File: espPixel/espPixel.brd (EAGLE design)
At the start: 39.3 x 80 mm, 68 parts, among them IC1 74LVC1T45GW,125, IC3 MP2315GJ-Z, IC4 CP2104, J1 TBLH10-350-04BK, J2 TBLH10-350-03BK, J3 TBLH10-350-02BK, Q1 SIR414DP-T1-GE3, Q2 SIR414DP-T1-GE3, Q5 mmbt2222, Q6 mmbt2222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

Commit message: bug fix
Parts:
- L1: value 4uh -> 1.5uh
- moved R11 1.80 mm to (15.7, 5.33), turned to 0 degrees
- moved R10 0.25 mm to (22.6, 4.32)
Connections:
- removed net N$7: C6.2, D1.A, U$1.1, U$1.2
- new net VDD: C6.2, D1.A, R12.1, U$1.1, U$1.2
- net VIN: no longer R12.1
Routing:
- net VDD: track 0.00 -> 14.6 mm, vias 0 -> 2
- net N$7: track 4.16 -> 0.00 mm
- net HSW: track 35.2 -> 31.0 mm, vias 30 -> 42
- net VIN: track 65.4 -> 63.9 mm, vias 52 -> 73
- net N$14: track 3.70 -> 3.15 mm
- net N$15: track 14.3 -> 14.8 mm
- net GND: vias 139 -> 152
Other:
- board text added: "V2.0"
- board text removed: "V1.0"

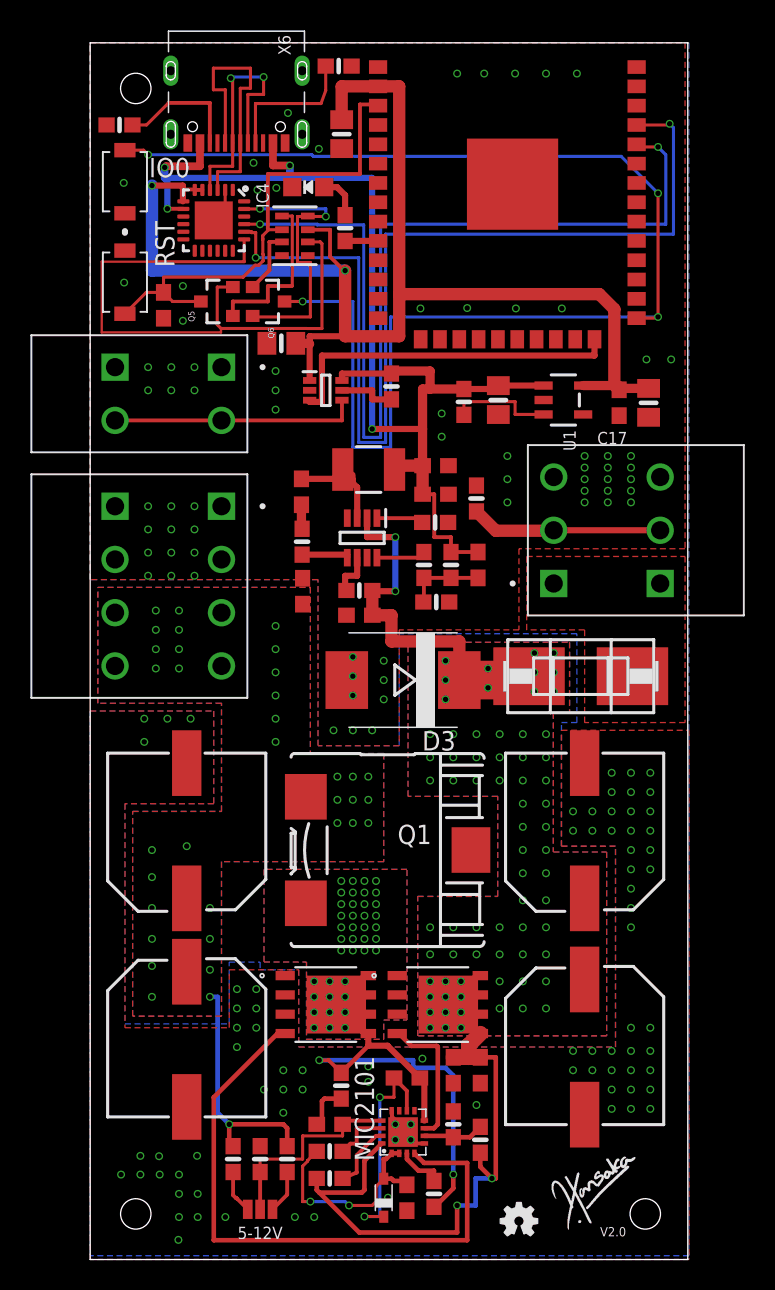
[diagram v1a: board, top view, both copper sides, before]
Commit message: Text clean up
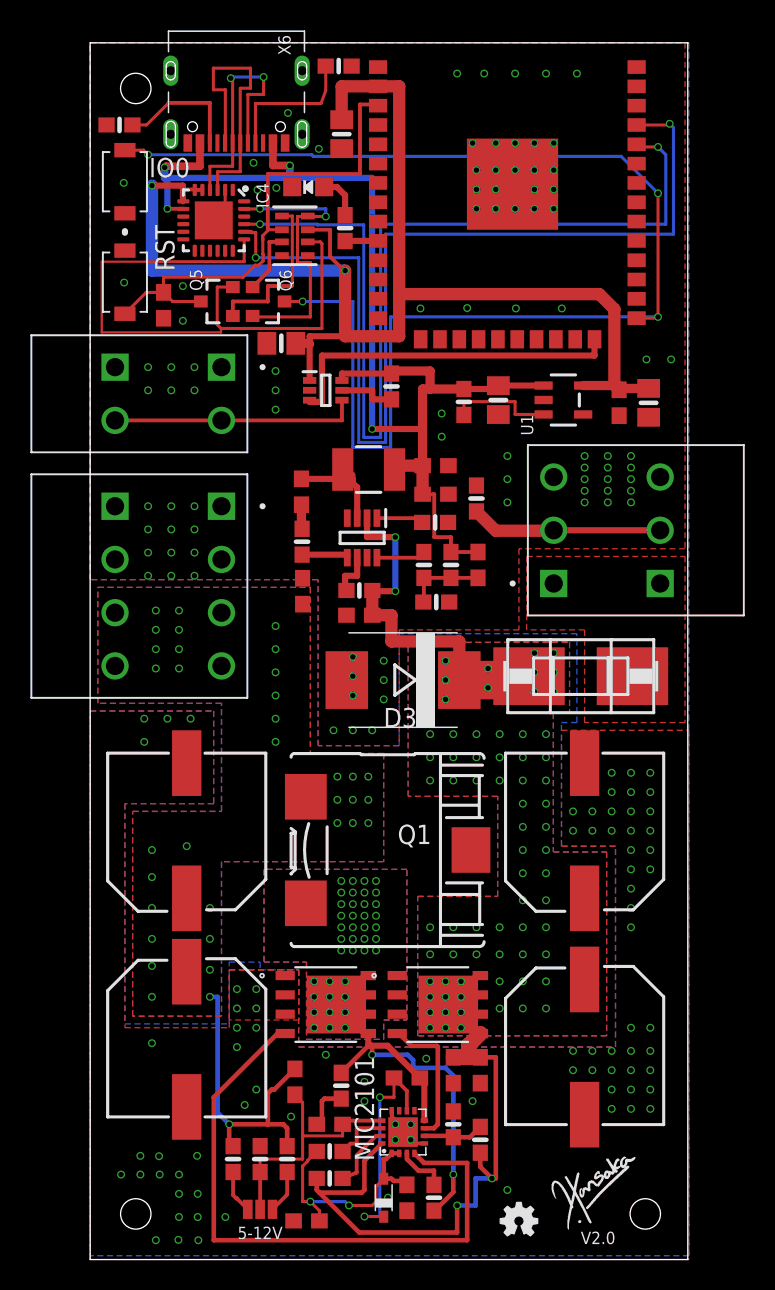
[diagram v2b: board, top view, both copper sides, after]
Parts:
- added C20: 0.4.7nf, microbuilder:0603-NO@1
- added C21: 4.7uf, microbuilder:0603-NO@1
- moved R10 0.25 mm to (22.6, 4.06)
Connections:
- net GND: now also C21.1
- net N$11: now also C20.1
- net VDD: now also C21.2
- net VOUT: now also C20.2
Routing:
- net VOUT: track 16.4 -> 20.8 mm
- net HSW: track 31.0 -> 26.7 mm
- net GND: track 5.91 -> 8.96 mm, vias 152 -> 171
- net N$11: track 13.7 -> 16.6 mm
- net VDD: track 14.6 -> 16.1 mm

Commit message: tunining
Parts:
- C20: value 0.4.7nf -> 4.7nf
- L1: value 1.5uh -> 4.7uh
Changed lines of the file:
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@@
 <attribute name="MOUSER_PRICE-STOCK" value="https://www.mouser.co.uk/ProductDetail/Nexperia/74LVC1T45GW125?qs=jquClx72t9Aoi%252BsTRKaaAg%3D%3D" x="37.084" y="10.16" size="1.778" layer="27" display="off"/>
 </element>
-<element name="L1" library="rcl" library_urn="urn:adsk.eagle:library:334" package="CEP125" package3d_urn="urn:adsk.eagle:package:25968/1" value="1.5uh" x="19.558" y="26.924" smashed="yes" rot="R90">
+<element name="L1" library="rcl" library_urn="urn:adsk.eagle:library:334" package="CEP125" package3d_urn="urn:adsk.eagle:package:25968/1" value="4.7uh" x="19.558" y="26.924" smashed="yes" rot="R90">
 <attribute name="POPULARITY" value="0" x="27.178" y="47.244" size="1.778" layer="27" rot="R90" display="off"/>
 <attribute name="SPICEPREFIX" value="L" x="27.178" y="47.244" size="1.778" layer="27" rot="R90" display="off"/>
@@
 <attribute name="PRICE" value="None" x="2.286" y="70.866" size="1.778" layer="27" rot="R90" display="off"/>
 </element>
-<element name="C20" library="microbuilder" package="0603-NO@1" value="0.4.7nf" x="13.462" y="11.684" smashed="yes" rot="R90">
+<element name="C20" library="microbuilder" package="0603-NO@1" value="4.7nf" x="13.462" y="11.684" smashed="yes" rot="R90">
 <attribute name="VALUE" x="12.7" y="9.906" size="0.8128" layer="27" font="vector" ratio="10" rot="R90"/>
 </element>

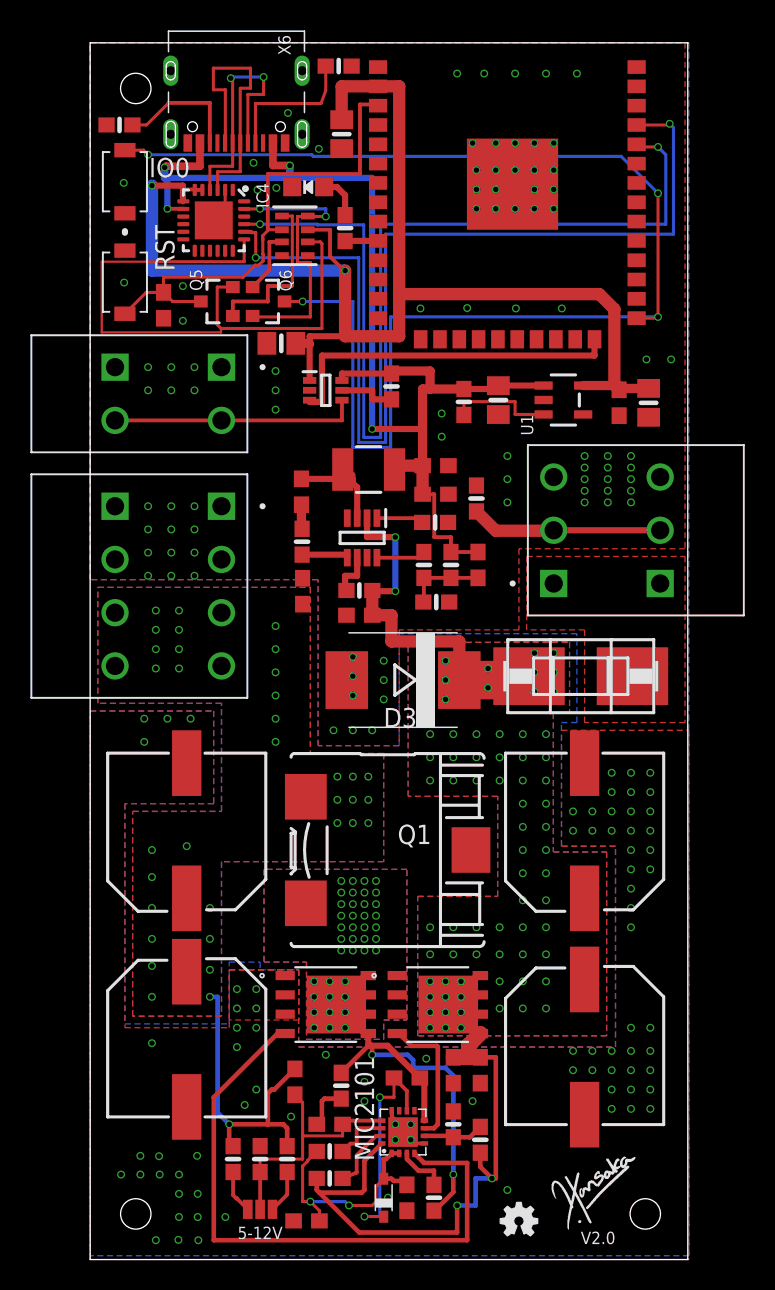
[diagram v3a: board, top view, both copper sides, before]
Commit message: ability to turn off the output
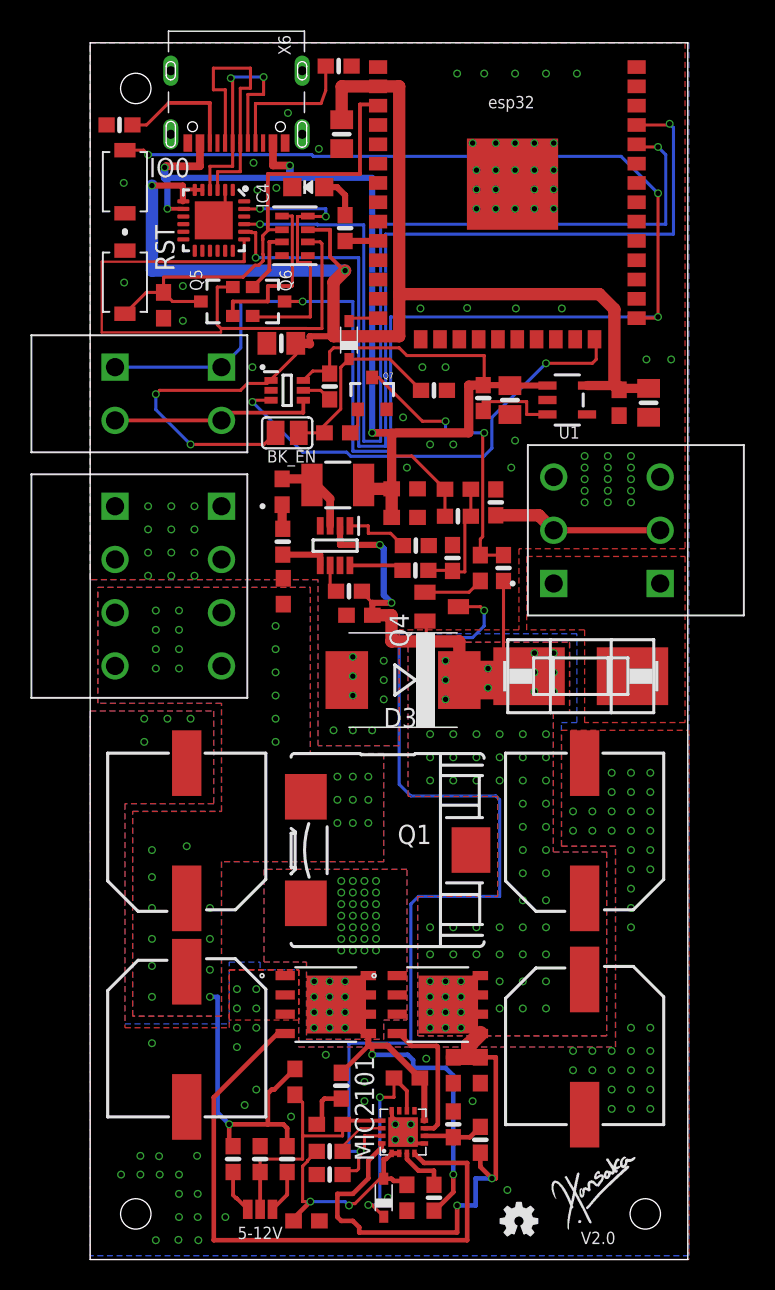
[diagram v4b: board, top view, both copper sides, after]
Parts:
- added BK_EN: (no value), jumper:SJ
- added D2: BAT60J, diode:SOD323_ST
- added Q4: (no value), semicon-smd-ipc:SOT23
- added Q7: mmbt2222, SparkFun:SOT23-3
- added R19: 1.2k, SparkFun-Resistors:0603
- added R20, R24, R25: 100K, microbuilder:0603-NO
- R16: value 50K -> 10
- R6: value 100K -> 1.2k; device microbuilder:0603-NO -> SparkFun-Resistors:0603
- moved R11 38.6 mm to (17.0, 43.9), turned to 180 degrees
- moved R6 10.5 mm to (16.3, 54.4)
- moved C10 5.15 mm to (24.2, 50.6), turned to 0 degrees
- moved R18 4.06 mm to (15.7, 57.4)
- moved R3 3.23 mm to (24.2, 48.9), turned to 0 degrees
- moved R4 3.09 mm to (23.8, 46.1), turned to 90 degrees
- moved C2 2.54 mm to (20.7, 50.7)
- moved C8 2.54 mm to (20.7, 48.8)
- moved IC1 2.54 mm to (13.0, 57.1)
- moved L3 2.27 mm to (16.3, 50.9)
- moved R1 1.98 mm to (21.4, 46.9)
- moved IC3 1.85 mm to (16.1, 46.9)
- moved R16 1.30 mm to (26.7, 49.8)
- moved R17 1.30 mm to (25.8, 56.6)
- moved C4 1.27 mm to (12.7, 43.9)
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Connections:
- removed net N$16: R11.2, U$1.15
- new net BUCK_EN: Q4.3, R25.1, U$1.15
- new net GPIO12: D2.A, X8.14
- new net N$23: Q7.1, R6.1
- new net N$24: Q4.1, R19.1
- new net N$26: Q7.3, R19.2, R24.1
- new net N$9: BK_EN.1, D2.C, R20.2, R6.2
- net 3.3V: now also BK_EN.2
- net GND: now also Q7.2, R20.1, R25.2; no longer J3.1_A, J3.1_B
- net GPIO0: now also J3.1_A, J3.1_B
- net N$5: now also R11.2; no longer R6.2
- net VIN: now also Q4.2, R24.2; no longer R6.1
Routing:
- net BUCK_EN: track 0.00 -> 63.4 mm, vias 0 -> 2
- net 3.3V: track 90.6 -> 110.0 mm, vias 2 -> 4
- net N$26: track 0.00 -> 19.0 mm, vias 0 -> 2
- net GPIO0: track 88.6 -> 105.0 mm
- net N$9: track 0.00 -> 12.9 mm
- net VBUS: track 76.8 -> 85.9 mm
- net NEODATA_3V: track 23.0 -> 30.6 mm, vias 0 -> 2
- net VIN: track 63.9 -> 71.2 mm
- net N$16: track 4.32 -> 0.00 mm
- net N$24: track 0.00 -> 3.95 mm
- net N$2: track 5.18 -> 8.29 mm
- net NEODATA_5V: track 16.2 -> 13.4 mm
- net GPIO12: track 0.00 -> 1.99 mm
- net N$22: track 3.85 -> 1.98 mm
- net N$23: track 0.00 -> 1.74 mm
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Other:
- board text added: "5V|12V"
- board text added: "8V-24V"
- board text added: "CK"
- board text added: "DATA"
- board text added: "GND"
- board text added: "PW-EN"
- board text added: "esp32"

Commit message: bigger caps
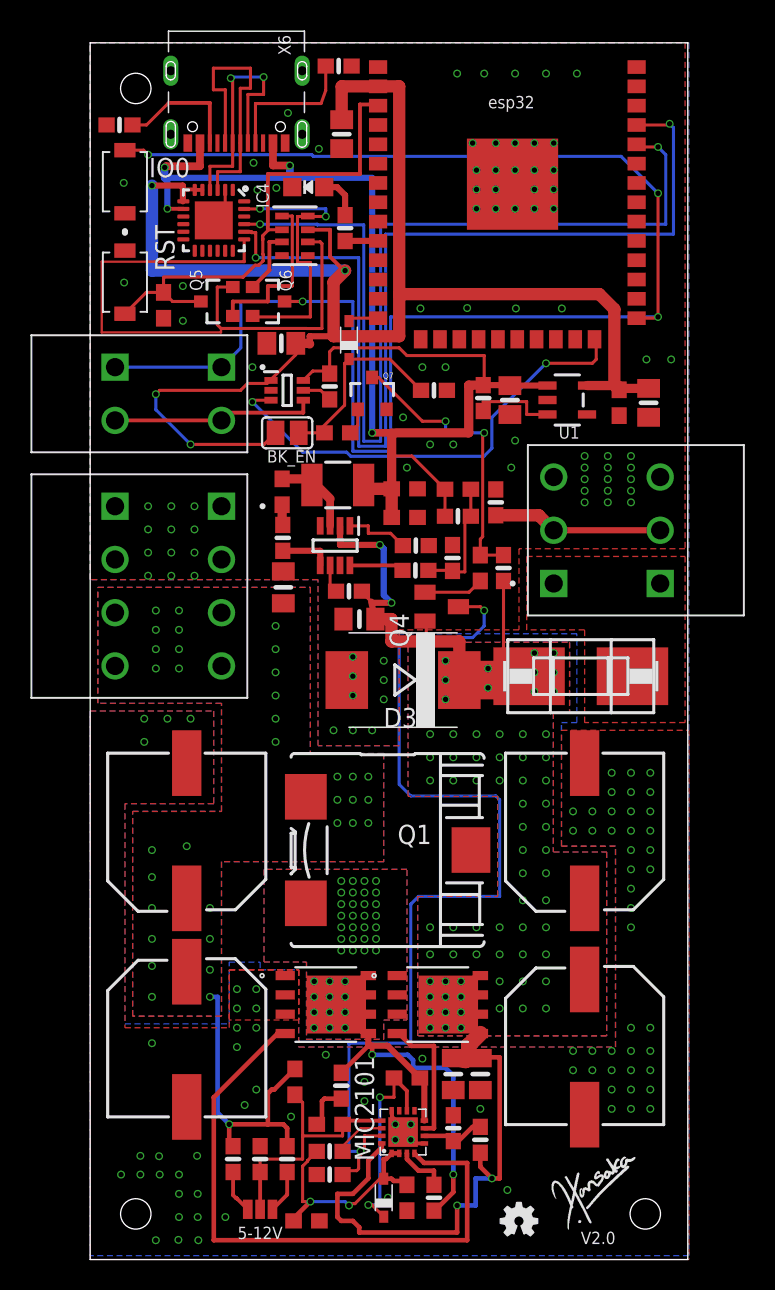
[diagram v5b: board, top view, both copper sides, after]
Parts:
- C12, C4, C7, C9: device microbuilder:0603-NO@1 -> microbuilder:0805_10MGAP
- moved C9 0.25 mm to (17.7, 42.1)
- moved R5 0.25 mm to (12.7, 47.5)
- moved R14 0.25 mm to (23.9, 8.64)
- moved C12 0.25 mm to (25.7, 12.2)
- moved C7 0.25 mm to (23.9, 12.2)
- moved C4 0.25 mm to (12.7, 44.2)

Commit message: clean up
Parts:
- added IC2: 74LVC1T45GW,125, 74LVC1T45GW_125:SOP65P210X110-6N
- added R26: 50K, microbuilder:0603-NO
- C11, C13, C14, C15: value 20uf -> 200uf; device rc-master-smd:CSV-G -> rc-master-smd:CSV-E/F
- moved J3 3.56 mm to (8.64, 55.1)
- moved J1 3.30 mm to (8.64, 46.2)
- moved F1 2.30 mm to (32.0, 36.1)
- moved J2 2.29 mm to (30.5, 42.2)
- moved C14 2.29 mm to (6.35, 25.9)
- moved C11 2.03 mm to (32.5, 26.2)
- moved RST 1.27 mm to (2.29, 63.0)
- moved IO0 1.27 mm to (2.29, 69.6)
- moved R21 1.14 mm to (2.44, 73.6)
- moved C15 0.76 mm to (6.35, 13.7)
- moved D3 0.76 mm to (20.6, 37.3)
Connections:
- new net GPIO0_5V: IC2.4, J3.1_A, J3.1_B
- new net N$16: IC2.5, R26.2
- net 3.3V: now also IC2.1
- net GND: now also IC2.2
- net GPIO0: now also IC2.3; no longer J3.1_A, J3.1_B
- net VBUS: now also IC2.6, R26.1
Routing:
- net VBUS: track 85.9 -> 106.2 mm, vias 4 -> 6
- net VOUT: track 20.8 -> 39.2 mm, vias 35 -> 51
- net GPIO0_5V: track 0.00 -> 16.8 mm
- net 3.3V: track 110.0 -> 120.4 mm
- net GPIO0: track 105.0 -> 98.7 mm, vias 4 -> 5
- net RESET: track 32.5 -> 38.2 mm, vias 0 -> 2
- net RTS: track 40.6 -> 35.0 mm
- net N$16: track 0.00 -> 4.52 mm
- net N$12: track 41.3 -> 44.5 mm
- net VIN: track 71.1 -> 68.7 mm, vias 73 -> 75
- net NEODATA_5V: track 13.4 -> 15.6 mm
- net N$19: track 11.3 -> 12.2 mm
- net BUCK_EN: track 63.4 -> 62.8 mm
- net HSW: vias 42 -> 45
- net GND: vias 166 -> 169
- added copper zone on layer 16, net N$20
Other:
- board text added: "V2"
- board text removed: "V2.0"

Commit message: finalizing the design
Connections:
- net GPIO12: now also R43.1
- net PW_LED: no longer R43.1
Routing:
- net GPIO12: track 1.99 -> 8.07 mm
- net PW_LED: track 2.18 -> 0.00 mm
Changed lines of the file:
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@@
 <setting verticaltext="up"/>
 </settings>
-<grid distance="10" unitdist="mil" unit="mil" style="lines" multiple="1" display="no" altdistance="5" altunitdist="mil" altunit="mil"/>
+<grid distance="2" unitdist="mil" unit="mil" style="lines" multiple="1" display="no" altdistance="5" altunitdist="mil" altunit="mil"/>
 <layers>
-<layer number="1" name="Top" color="4" fill="1" visible="no" active="yes"/>
+<layer number="1" name="Top" color="4" fill="1" visible="yes" active="yes"/>
 <layer number="16" name="Bottom" color="1" fill="1" visible="yes" active="yes"/>
 <layer number="17" name="Pads" color="2" fill="1" visible="yes" active="yes"/>
@@
 <contactref element="U1" pad="3"/>
 <wire x1="30.0689" y1="55.565" x2="28.702" y2="55.565" width="0.2032" layer="1"/>
-<wire x1="28.702" y1="56.4086" x2="25.8445" y2="56.4086" width="0.2032" layer="1"/>
-<wire x1="25.8445" y1="56.4086" x2="25.8445" y2="55.792" width="0.2032" layer="1"/>
-<wire x1="28.702" y1="55.565" x2="28.702" y2="56.4086" width="0.2032" layer="1"/>
+<wire x1="28.702" y1="56.5102" x2="25.8445" y2="56.5102" width="0.2032" layer="1"/>
+<wire x1="25.8445" y1="56.5102" x2="25.8445" y2="55.792" width="0.2032" layer="1"/>
+<wire x1="28.702" y1="55.565" x2="28.702" y2="56.5102" width="0.2032" layer="1"/>
 </signal>
 <signal name="RESET">
@@
 <signal name="PW_LED">
 <contactref element="X8" pad="10"/>
-<contactref element="R43" pad="1"/>
-<wire x1="18.932" y1="66.976" x2="16.764" y2="66.976" width="0.4064" layer="1"/>
-<wire x1="16.764" y1="66.976" x2="16.764" y2="66.968" width="0.4064" layer="1"/>
 </signal>
 <signal name="D+">
@@
 <contactref element="X8" pad="14"/>
 <contactref element="D2" pad="A"/>
-<wire x1="18.932" y1="61.896" x2="17.212" y2="61.896" width="0.2032" layer="1"/>
-<wire x1="17.212" y1="61.896" x2="17.018" y2="61.702" width="0.2032" layer="1"/>
+<wire x1="17.212" y1="61.896" x2="17.1296" y2="61.8136" width="0.2032" layer="1"/>
+<contactref element="R43" pad="1"/>
+<wire x1="17.1296" y1="61.8136" x2="17.018" y2="61.702" width="0.2032" layer="1"/>
+<wire x1="16.764" y1="66.968" x2="17.7292" y2="66.0028" width="0.4064" layer="1"/>
+<wire x1="17.7292" y1="62.4132" x2="17.1296" y2="61.8136" width="0.4064" layer="1"/>
+<wire x1="17.7292" y1="66.0028" x2="17.7292" y2="62.4132" width="0.4064" layer="1"/>
+<wire x1="18.932" y1="61.896" x2="17.212" y2="61.896" width="0.4064" layer="1"/>
+<wire x1="17.212" y1="61.896" x2="17.018" y2="61.702" width="0.4064" layer="1"/>
 </signal>
 <signal name="N$23">

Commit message: More filter caps
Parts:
- added C22, C25: 0.1uF, microbuilder:0603-NO@1
- added C23: 1uF, microbuilder:0603-NO@1
- added C24, C26: 47uf, adafruit:C3225
- moved C4 9.89 mm to (14.3, 34.4), turned to 180 degrees
- moved U$33 2.16 mm to (31.8, 2.29)
- moved C6 1.94 mm to (20.6, 5.99)
- moved D1 1.63 mm to (19.3, 5.69)
- moved U$1 1.47 mm to (20.5, 9.86)
- moved R10 1.43 mm to (22.2, 5.44)
- moved C3 1.03 mm to (15.9, 9.91)
- moved R7 1.02 mm to (16.6, 12.4)
- moved C5 0.82 mm to (20.7, 12.8)
- moved C21 0.79 mm to (14.4, 3.30)
- moved R12 0.76 mm to (15.7, 7.87)
- moved R25 0.76 mm to (16.0, 6.30)
- moved C13 0.61 mm to (32.5, 13.4)
- moved C15 0.41 mm to (6.40, 13.3)
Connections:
- net GND: now also C22.1, C23.1, C24.2, C25.2, C26.2
- net VIN: now also C25.1
- net VOUT: now also C22.2, C23.2, C24.1, C26.1
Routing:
- net VOUT: track 39.2 -> 35.1 mm, vias 51 -> 59
- net VIN: track 68.7 -> 72.0 mm
- net N$12: track 44.5 -> 41.4 mm
- net HSW: track 26.7 -> 24.0 mm
- net BUCK_EN: track 62.8 -> 60.9 mm
- net VDD: track 15.8 -> 17.5 mm
- net N$15: track 13.9 -> 15.3 mm
- net GND: track 8.96 -> 10.3 mm, vias 169 -> 198
- net FREQ: track 4.37 -> 5.55 mm
- net N$13: track 8.80 -> 7.83 mm
- net N$8: track 3.00 -> 2.40 mm
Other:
- board text added: "V3"
- board text removed: "V2"
